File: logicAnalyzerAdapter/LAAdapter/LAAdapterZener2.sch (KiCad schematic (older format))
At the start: 19 parts, among them J1 Conn_02x05_Odd_Even, J2 Conn_01x08_Male

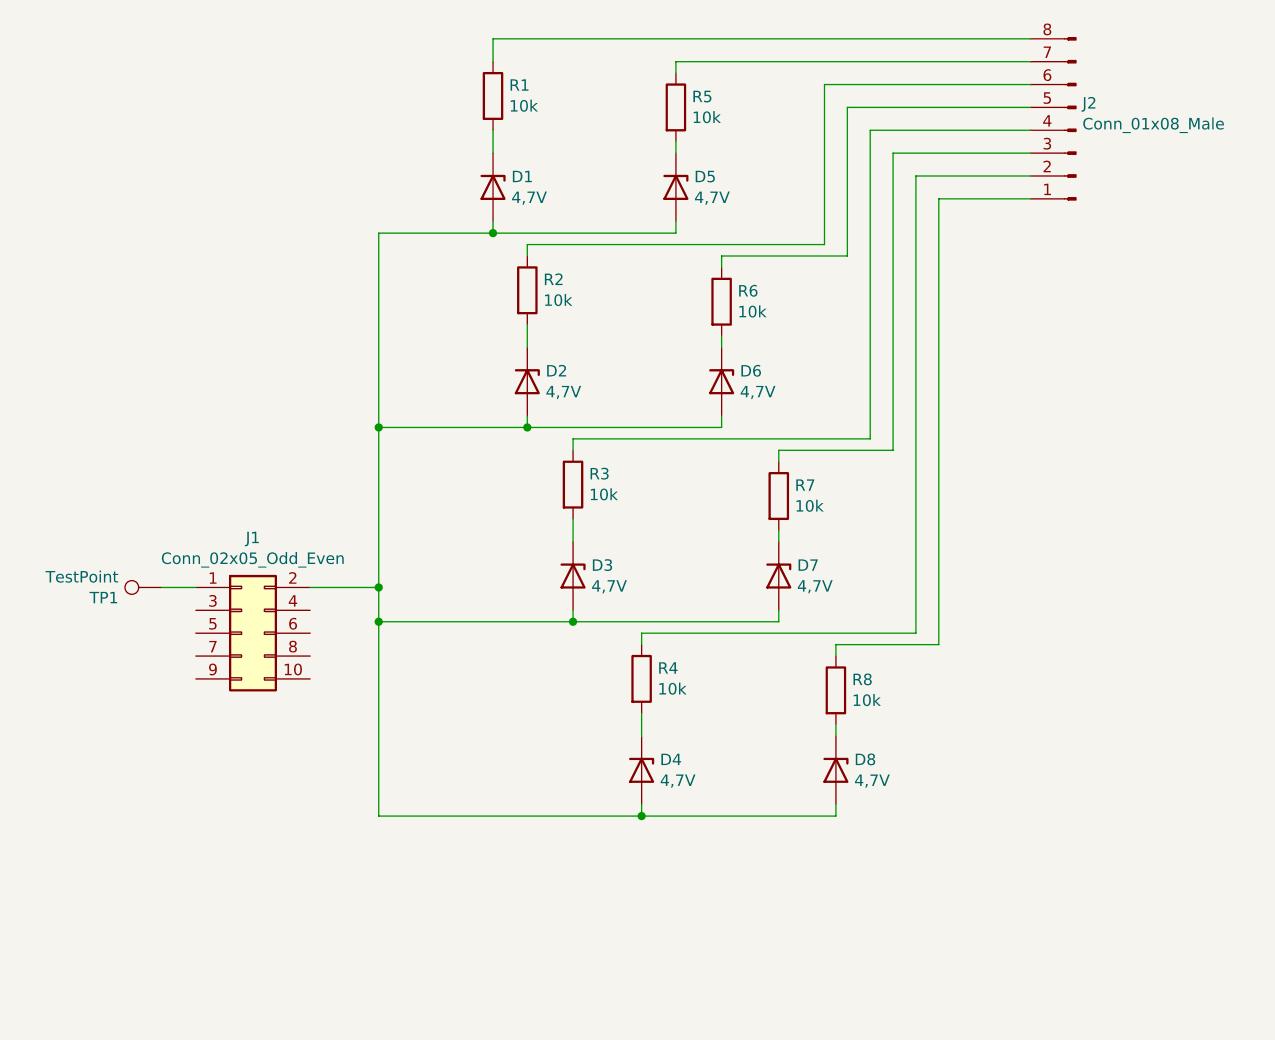
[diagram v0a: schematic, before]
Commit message: nová zenerková verze pro všech 8 kanálů
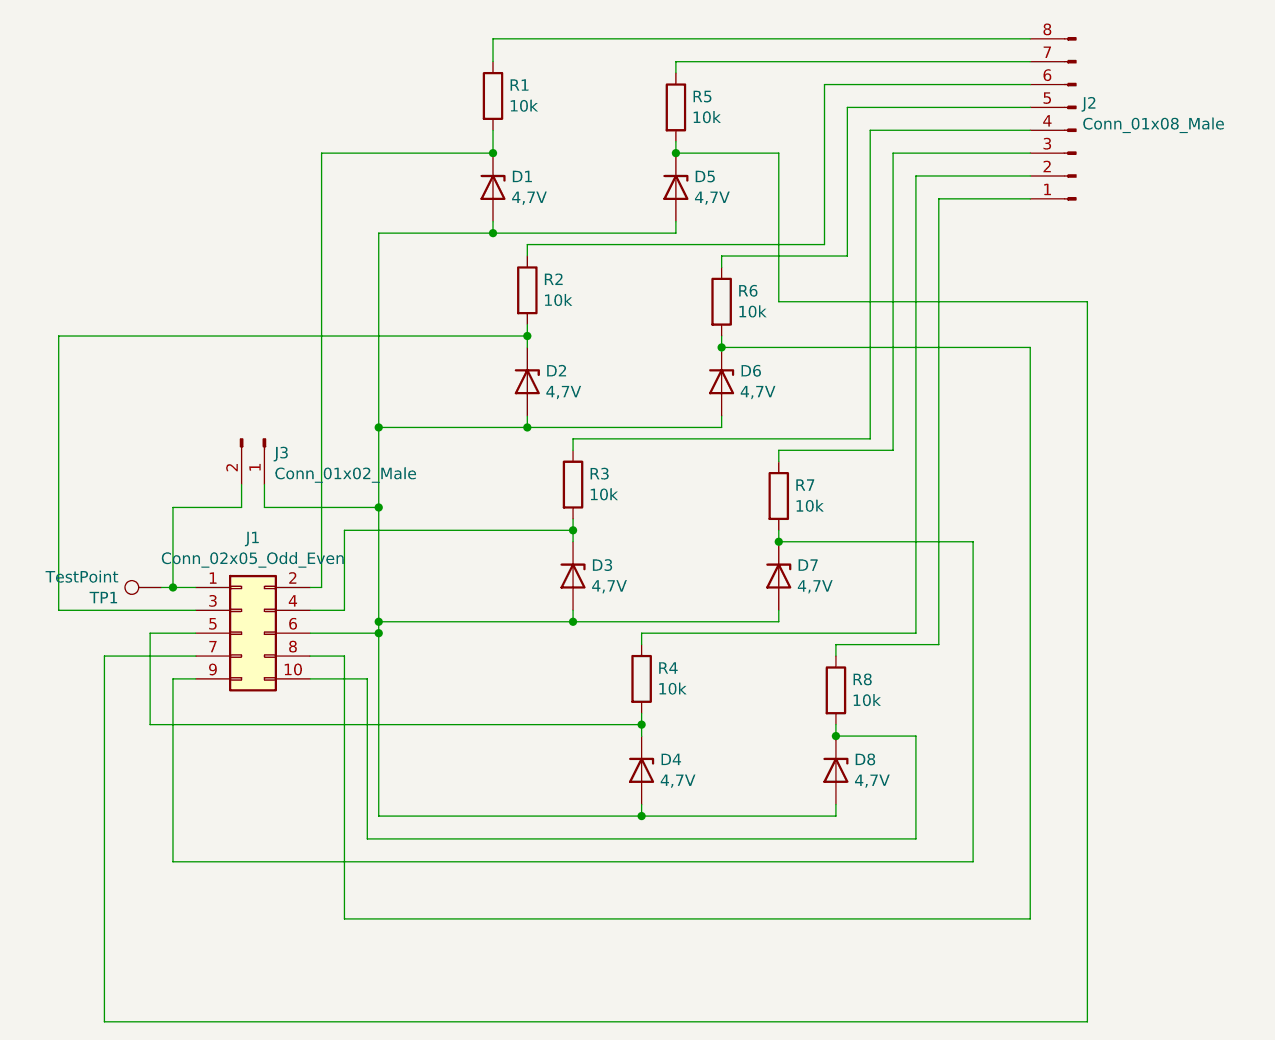
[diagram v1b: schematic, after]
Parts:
- added J3: Conn_01x02_Male, Jumper:SolderJumper-2_P1.3mm_Open_TrianglePad1.0x1.5mm, symbol Connector:Conn_01x02_Male
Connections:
- net at D5.1 (K), R5.2: now also J1.7 (Pin_7)
- net at D1.2 (A), D2.2 (A), D3.2 (A)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: now also J1.6 (Pin_6), J3.1 (Pin_1); no longer J1.2 (Pin_2)
- net at J1.1 (Pin_1), TP1.1: now also J3.2 (Pin_2)
- net at J1.10 (Pin_10): now also D8.1 (K), R8.2
- net at J1.3 (Pin_3): now also D2.1 (K), R2.2
- net at J1.4 (Pin_4): now also D3.1 (K), R3.2
- net at J1.5 (Pin_5): now also D4.1 (K), R4.2
- net at J1.8 (Pin_8): now also D6.1 (K), R6.2
- net at J1.9 (Pin_9): now also D7.1 (K), R7.2
- net at D1.1 (K), R1.2: now also J1.2 (Pin_2)
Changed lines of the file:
@@
 $EndComp
 Wire Wire Line
-	2900 3050 2750 3050
+	2900 3050 2800 3050
 $Comp
 L Device:D_Zener D5
@@
 $EndComp
 Wire Wire Line
-	4350 1900 4350 2000
+	4350 1900 4350 1950
 $Comp
 L Device:D_Zener D3
@@
 $EndComp
 Wire Wire Line
-	4550 2750 4550 2850
+	4550 2750 4550 2800
 $Comp
 L Device:D_Zener D4
@@
 $EndComp
 Wire Wire Line
-	4850 3600 4850 3700
+	4850 3600 4850 3650
 Wire Wire Line
 	4200 750  4200 650
@@
 Wire Wire Line
 	3700 1500 3700 2350
-Wire Wire Line
-	3700 3050 3400 3050
 Wire Wire Line
 	5000 1450 5000 1500
@@
 Connection ~ 3700 2350
 Wire Wire Line
-	3700 2350 3700 3050
-Wire Wire Line
 	4350 2300 4350 2350
 Connection ~ 4350 2350
@@
 	5450 3200 4550 3200
 Wire Wire Line
-	3700 3200 3700 3050
-Connection ~ 3700 3050
-Wire Wire Line
 	4550 3150 4550 3200
 Connection ~ 4550 3200
@@
 	5700 4050 4850 4050
 Wire Wire Line
-	3700 4050 3700 3200
+	3700 4050 3700 3250
 Connection ~ 3700 3200
 Wire Wire Line
@@
 Wire Wire Line
 	4850 4050 3700 4050
+Wire Wire Line
+	5700 3700 6050 3700
+Wire Wire Line
+	6050 3700 6050 4150
+Wire Wire Line
+	6050 4150 3650 4150
+Wire Wire Line
+	3650 4150 3650 3450
+Wire Wire Line
+	3650 3450 3400 3450
+Connection ~ 5700 3700
+Wire Wire Line
+	3700 2350 3700 2700
+Wire Wire Line
+	3400 3250 3700 3250
+Connection ~ 3700 3250
+Wire Wire Line
+	3700 3250 3700 3200
+Wire Wire Line
+	4850 3650 2700 3650
+Wire Wire Line
+	2700 3650 2700 3250
+Wire Wire Line
+	2700 3250 2900 3250
+Connection ~ 4850 3650
+Wire Wire Line
+	4850 3650 4850 3700
+Wire Wire Line
+	5450 2850 6300 2850
+Wire Wire Line
+	6300 2850 6300 4250
+Wire Wire Line
+	6300 4250 2800 4250
+Wire Wire Line
+	2800 4250 2800 3450
+Wire Wire Line
+	2800 3450 2900 3450
+Connection ~ 5450 2850
+Wire Wire Line
+	4550 2800 3550 2800
+Wire Wire Line
+	3550 2800 3550 3150
+Wire Wire Line
+	3550 3150 3400 3150
+Connection ~ 4550 2800
+Wire Wire Line
+	4550 2800 4550 2850
+Wire Wire Line
+	5200 2000 6550 2000
+Wire Wire Line
+	6550 2000 6550 4500
+Wire Wire Line
+	6550 4500 3550 4500
+Wire Wire Line
+	3550 4500 3550 3350
+Wire Wire Line
+	3550 3350 3400 3350
+Connection ~ 5200 2000
+Wire Wire Line
+	4350 1950 2300 1950
+Wire Wire Line
+	2300 1950 2300 3150
+Wire Wire Line
+	2300 3150 2900 3150
+Connection ~ 4350 1950
+Wire Wire Line
+	4350 1950 4350 2000
+Wire Wire Line
+	5000 1150 5450 1150
+Wire Wire Line
+	5450 1150 5450 1800
+Wire Wire Line
+	5450 1800 6800 1800
+Wire Wire Line
+	6800 1800 6800 4950
+Wire Wire Line
+	6800 4950 2500 4950
+Wire Wire Line
+	2500 4950 2500 3350
+Wire Wire Line
+	2500 3350 2900 3350
+Connection ~ 5000 1150
+Wire Wire Line
+	3400 3050 3450 3050
+Wire Wire Line
+	3450 1150 4200 1150
+Connection ~ 4200 1150
+$Comp
+L Connector:Conn_01x02_Male J3
+U 1 1 6058FD8E
+P 3200 2400
+F 0 "J3" V 3262 2444 50  0000 L CNN
+F 1 "Conn_01x02_Male" V 3353 2444 50  0000 L CNN
+F 2 "Jumper:SolderJumper-2_P1.3mm_Open_TrianglePad1.0x1.5mm" H 3200 2400 50  0001 C CNN
+F 3 "~" H 3200 2400 50  0001 C CNN
+	1    3200 2400
+	0    1    1    0
+$EndComp
+Wire Wire Line
+	2800 3050 2800 2700
+Wire Wire Line
+	2800 2700 3100 2700
+Wire Wire Line
+	3100 2700 3100 2600
+Connection ~ 2800 3050
+Wire Wire Line
+	2800 3050 2750 3050
+Wire Wire Line
+	3200 2600 3200 2700
+Wire Wire Line
+	3450 1150 3450 3050
+Wire Wire Line
+	3200 2700 3700 2700
+Connection ~ 3700 2700
+Wire Wire Line
+	3700 2700 3700 3200
 $EndSCHEMATC
